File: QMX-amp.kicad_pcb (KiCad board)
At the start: 2 copper layers, 94 x 125 mm, 108 parts, among them J1 Conn_01x08_Pin, J2 RF-IN, J3 RF-OUT, J4 Barrel_Jack_Switch, K1 EA2-5NU, K10 HK19F-DCxxV-SHC, K11 EA2-5NU, K12 EA2-5NU, K13 EA2-5NU, K14 EA2-5NU, K2 EA2-5NU, K3 EA2-5NU, K4 EA2-5NU, K5 EA2-5NU, K6 EA2-5NU, K7 EA2-5NU, K8 EA2-5NU, K9 HK19F-DCxxV-SHC, Q1 BSS123, Q2 BSS123, Q3 BSS123, Q4 BSS123, Q5 BSS123, Q6 MPS-751, Q7 BSS123, Q8 BSS123, T1 BN-43-202, U1 SJ1-3523N, U2 LM7805_TO220, U3 RD16HHF1, U4 RD16HHF1

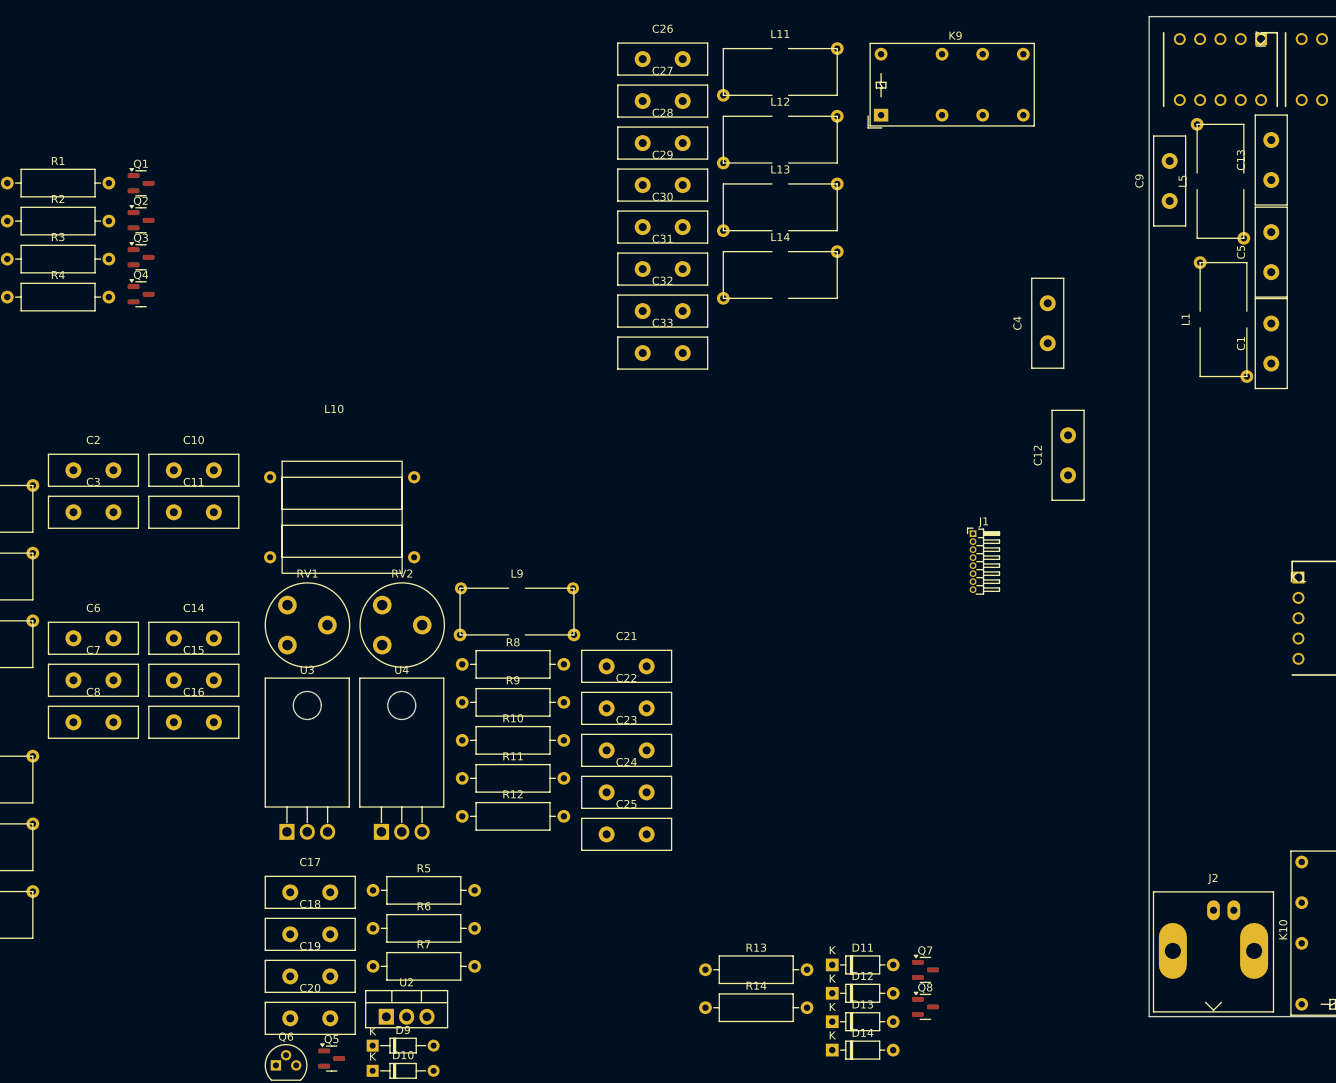
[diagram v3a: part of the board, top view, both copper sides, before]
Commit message: v0.10 after slimming down capacitor width to 3mm so it *barely* fits.
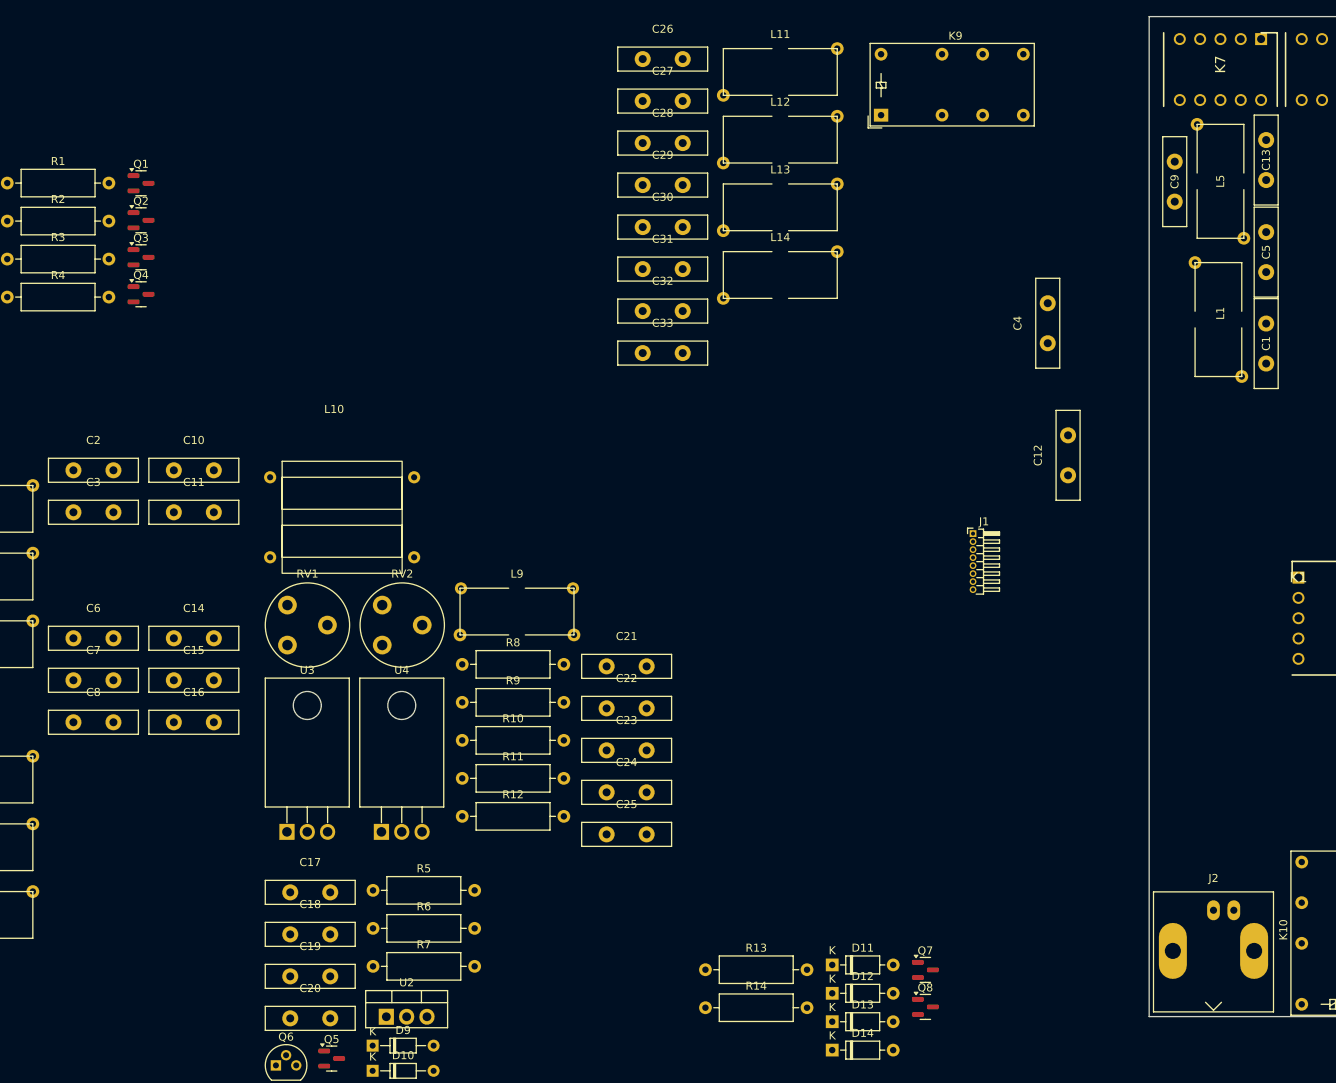
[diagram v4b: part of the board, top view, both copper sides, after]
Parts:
- C1, C10, C11, C12, C13, C14, C15, C16, C17, C18, C19, C2, C20, C21, C22, C23, C24, C25, C26, C27, C28, C29, C3, C30, C31, C32, C33, C4, C5, C6, C7, C8, C9: footprint ZZZMyLibrary:C_Disc_D11.0mm_W4.0mm_P5.00mm -> ZZZMyLibrary:C_Disc_D11.0mm_W3.0mm_P5.00mm
- moved C9 0.64 mm to (102.2, 53.3)
- moved L1 0.64 mm to (105.0, 68.1)
- moved C1 0.63 mm to (113.7, 73.6)
- moved C13 0.63 mm to (113.7, 50.6)
- moved C5 0.63 mm to (113.7, 62.1)
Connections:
- net K1-14 renamed K10-14
- net K2-14 renamed K9-14

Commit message: whatever changes happened?
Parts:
- moved L8 218.0 mm to (151.0, 50.2), turned to 90 degrees
- moved C8 203.0 mm to (159.4, 61.5), turned to 90 degrees
- moved L4 202.0 mm to (150.8, 68.1), turned to 90 degrees
- moved L7 200.7 mm to (135.9, 50.2), turned to 90 degrees
- moved C16 194.7 mm to (159.4, 50.1), turned to 90 degrees
- moved C7 186.9 mm to (144.1, 61.5), turned to 90 degrees
- moved L3 185.5 mm to (135.5, 68.1), turned to 90 degrees
- moved L6 182.9 mm to (120.2, 50.2), turned to 90 degrees
- moved C3 180.6 mm to (144.1, 72.9), turned to 90 degrees
- moved C15 178.5 mm to (144.1, 50.1), turned to 90 degrees
- moved C6 170.8 mm to (128.9, 61.5), turned to 90 degrees
- moved L2 169.2 mm to (120.3, 68.1), turned to 90 degrees
- moved C2 164.9 mm to (128.9, 72.9), turned to 90 degrees
- moved C14 162.4 mm to (128.9, 50.1), turned to 90 degrees
- moved C11 160.4 mm to (132.7, 53.3), turned to 90 degrees
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
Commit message: Ron helped moved all the parts into PCB
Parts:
- removed D10: 1N4148, Diode_THT:D_DO-34_SOD68_P7.62mm_Horizontal
- removed D13, D14, D5, D6, D7, D8: 1N4148, Diode_THT:D_DO-35_SOD27_P7.62mm_Horizontal
- C18, C19, C20, C21, C22, C23, C24: footprint ZZZMyLibrary:C_Disc_D11.0mm_W3.0mm_P5.00mm -> Resistor_SMD:R_0805_2012Metric_Pad1.20x1.40mm_HandSolder
- L10: footprint ZZZMyLibrary:BN-43-202-FLAT -> ZZZMyLibrary:BN-43-7051-FLAT
- R1, R11, R12, R13, R14, R2, R3, R4, R5, R6, R7: footprint Resistor_THT:R_Axial_DIN0309_L9.0mm_D3.2mm_P12.70mm_Horizontal -> Resistor_SMD:R_0805_2012Metric_Pad1.20x1.40mm_HandSolder
- R10, R8, R9: footprint Resistor_THT:R_Axial_DIN0309_L9.0mm_D3.2mm_P12.70mm_Horizontal -> Resistor_THT:R_Axial_DIN0207_L6.3mm_D2.5mm_P2.54mm_Vertical
- moved D4 208.6 mm to (151.1, 96.5), turned to 90 degrees
- moved R4 206.5 mm to (161.3, 90.4), turned to 90 degrees
- moved C19 199.0 mm to (187.0, 111.8)
- moved D3 194.3 mm to (135.9, 96.5), turned to 90 degrees
- moved R3 192.1 mm to (146.1, 90.2), turned to 90 degrees
- moved C20 186.7 mm to (170.4, 101.6)
- moved Q4 186.5 mm to (157.8, 90.2), turned to 180 degrees
- moved RV1 180.5 mm to (171.5, 119.3)
- moved D2 180.2 mm to (120.7, 96.5), turned to 90 degrees
- moved R2 177.9 mm to (130.8, 90.2), turned to 90 degrees
- moved U2 177.9 mm to (171.4, 96.2)
- moved Q3 172.2 mm to (142.6, 90.2), turned to 180 degrees
- moved RV2 169.7 mm to (171.4, 130.7)
- moved Q5 167.1 mm to (152.7, 100.3)
- moved D1 166.4 mm to (105.4, 96.5), turned to 90 degrees
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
